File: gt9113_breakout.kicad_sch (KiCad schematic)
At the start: 10 parts, among them J6 504740-5100, J7 504740-5100, U9 GT9113

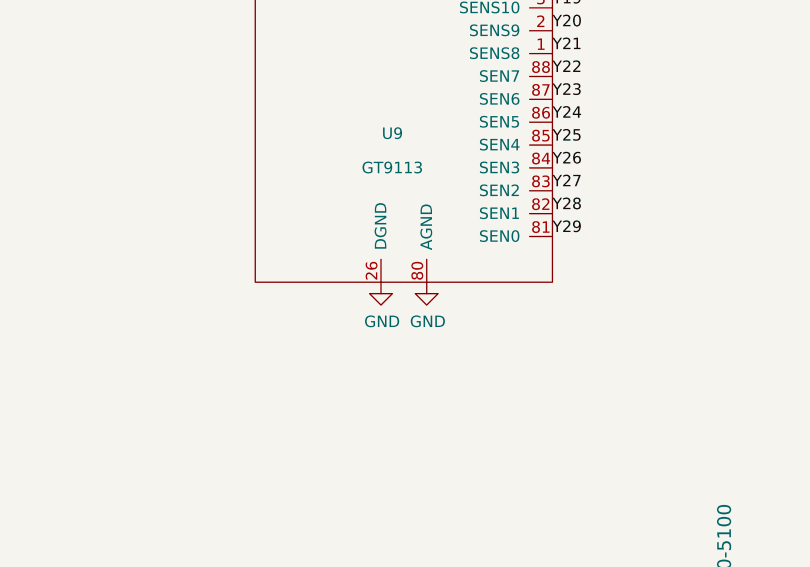
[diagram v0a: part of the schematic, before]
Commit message: Route CM4 board with differential connector on the right.
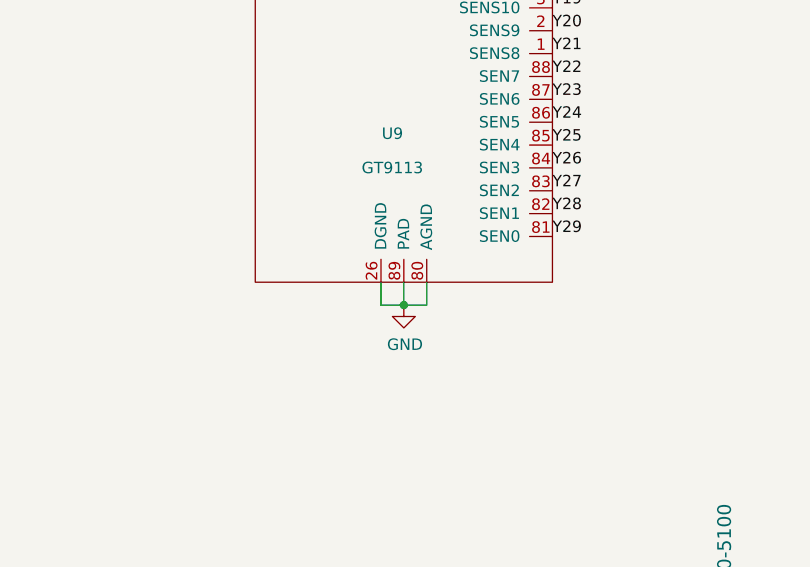
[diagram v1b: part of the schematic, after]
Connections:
- net GND: now also U9.89 (PAD)

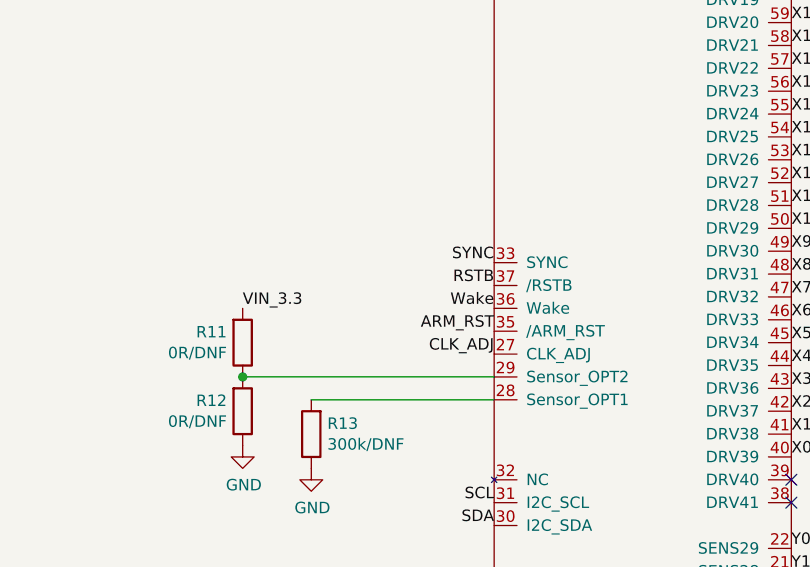
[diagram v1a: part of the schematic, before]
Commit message: Lots of tiny test points; add 3d models to a bunch of things. Re-length-match PCIe and DSI traces.
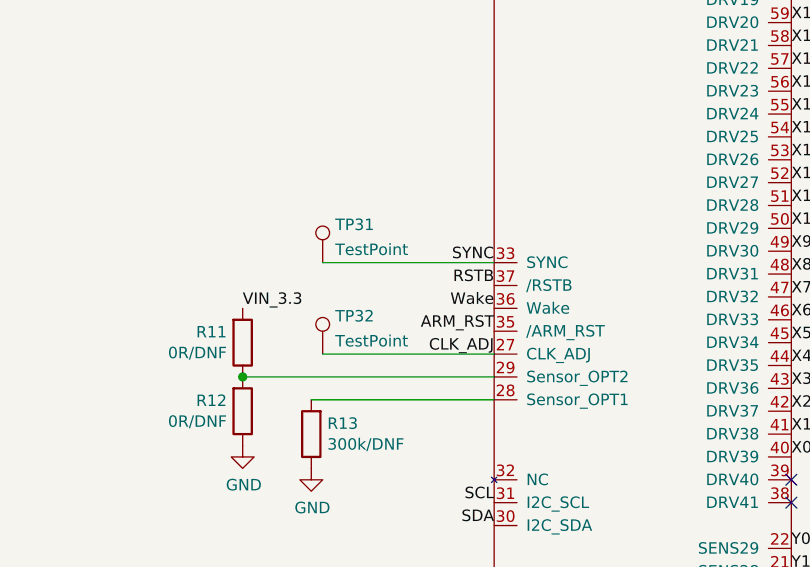
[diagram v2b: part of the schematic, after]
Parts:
- added TP31, TP32: TestPoint, footprints:testpoint_small, symbol Connector:TestPoint
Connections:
- net CLK_ADJ: now also TP32.1
- net SYNC: now also TP31.1
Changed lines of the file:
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@@
     (stroke (width 0) (type solid) (color 0 0 0 0))
+  )
+  (wire (pts (xy 214.63 137.16) (xy 233.68 137.16))
+    (stroke (width 0) (type default) (color 0 0 0 0))
   )
   (wire (pts (xy 247.65 44.45) (xy 247.65 24.13))
@@
   (wire (pts (xy 233.68 142.24) (xy 213.36 142.24))
     (stroke (width 0) (type solid) (color 0 0 0 0))
+  )
+  (wire (pts (xy 214.63 127) (xy 233.68 127))
+    (stroke (width 0) (type default) (color 0 0 0 0))
   )
   (wire (pts (xy 250.19 26.67) (xy 250.19 44.45))
@@
       (effects (font (size 1.27 1.27)) hide)
     )
+    (pin "1")
+  )
+  (symbol (lib_id "Connector:TestPoint") (at 214.63 127 0) (unit 1)
+    (in_bom yes) (on_board yes) (fields_autoplaced)
+    (property "Reference" "TP31" (id 0) (at 216.027 122.7895 0)
+      (effects (font (size 1.27 1.27)) (justify left))
+    )
+    (property "Value" "TestPoint" (id 1) (at 216.027 125.5646 0)
+      (effects (font (size 1.27 1.27)) (justify left))
+    )
+    (property "Footprint" "footprints:testpoint_small" (id 2) (at 219.71 127 0)
+      (effects (font (size 1.27 1.27)) hide)
+    )
+    (property "Datasheet" "~" (id 3) (at 219.71 127 0)
+      (effects (font (size 1.27 1.27)) hide)
+    )
+    (pin "1")
+  )
+  (symbol (lib_id "Connector:TestPoint") (at 214.63 137.16 0) (unit 1)
+    (in_bom yes) (on_board yes) (fields_autoplaced)
+    (property "Reference" "TP32" (id 0) (at 216.027 132.9495 0)
+      (effects (font (size 1.27 1.27)) (justify left))
+    )
+    (property "Value" "TestPoint" (id 1) (at 216.027 135.7246 0)
+      (effects (font (size 1.27 1.27)) (justify left))
+    )
+    (property "Footprint" "footprints:testpoint_small" (id 2) (at 219.71 137.16 0)
+      (effects (font (size 1.27 1.27)) hide)
+    )
+    (property "Datasheet" "~" (id 3) (at 219.71 137.16 0)
+      (effects (font (size 1.27 1.27)) hide)
+    )

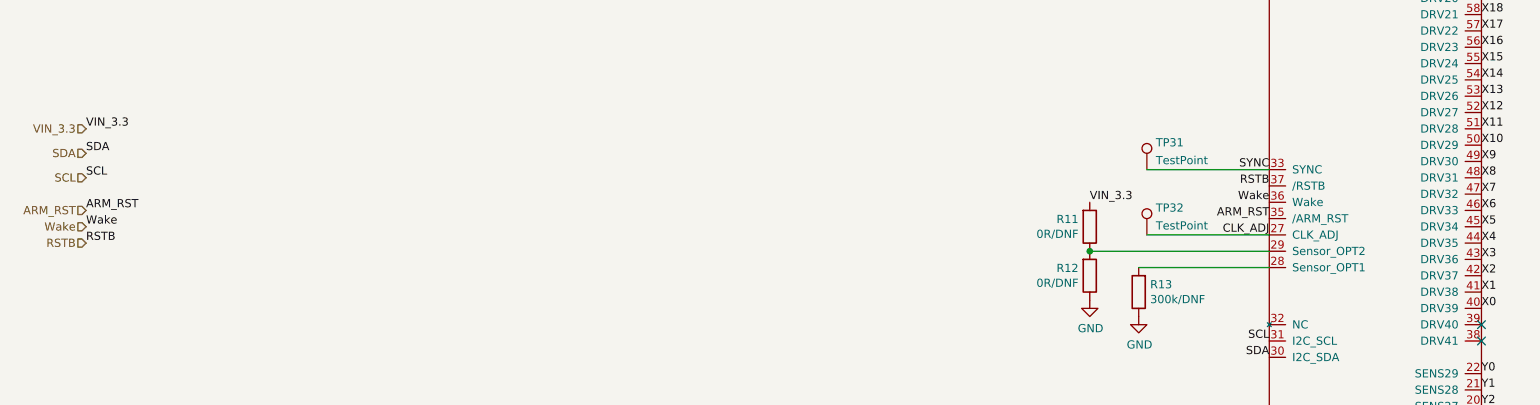
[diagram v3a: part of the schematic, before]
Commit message: Wire GT9110 INT pin to a GPIO, wire ARM_RST and Wake pins to test points instead of GPIOs. Add lots of test points, and footprints for status/power LEDs.
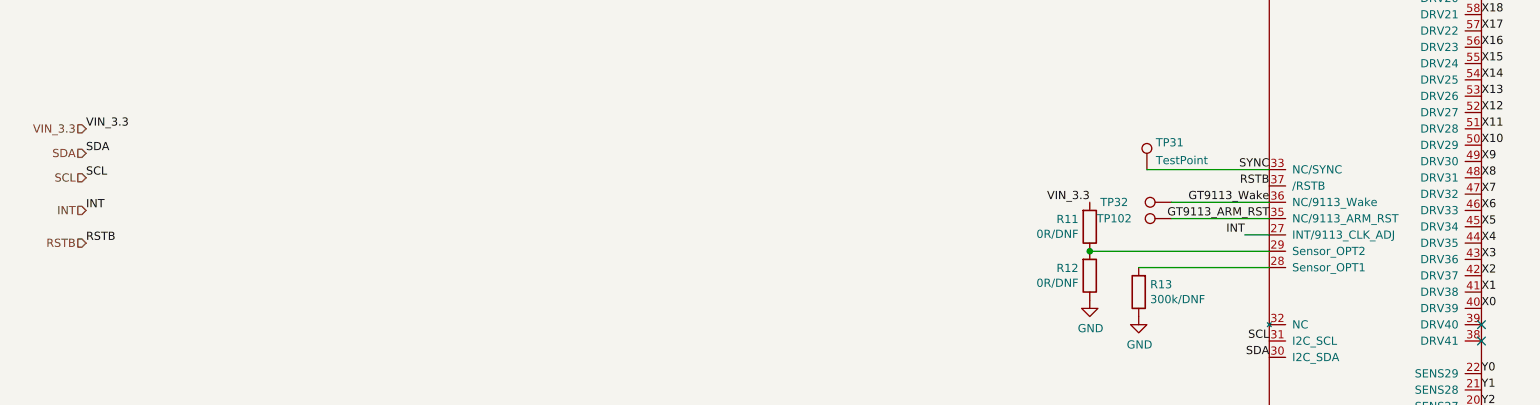
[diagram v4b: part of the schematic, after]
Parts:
- added TP102: TestPoint, footprints:testpoint_small, symbol Connector:TestPoint
- U9: symbol gt9113:GT9113 -> gt9113:GT9110
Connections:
- net Wake is gone; now on net GT9113_Wake: U9.36 (NC/9113_Wake)
- net ARM_RST renamed GT9113_ARM_RST
- net GT9113_ARM_RST: now also TP102.1
- net CLK_ADJ renamed GT9113_Wake
- net GT9113_Wake: no longer U9.27 (CLK_ADJ)
- new net INT: U9.27 (INT/9113_CLK_ADJ)
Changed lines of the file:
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@@
+    (stroke (width 0) (type default) (color 0 0 0 0))
+  )
+  (wire (pts (xy 218.44 134.62) (xy 233.68 134.62))
+    (stroke (width 0) (type default) (color 0 0 0 0))
+  )
+  (wire (pts (xy 229.87 137.16) (xy 233.68 137.16))
     (stroke (width 0) (type default) (color 0 0 0 0))
   )
@@
     (stroke (width 0) (type solid) (color 0 0 0 0))
   )
-  (wire (pts (xy 214.63 137.16) (xy 233.68 137.16))
-    (stroke (width 0) (type default) (color 0 0 0 0))
-  )
   (wire (pts (xy 247.65 44.45) (xy 247.65 24.13))
     (stroke (width 0) (type solid) (color 0 0 0 0))
@@
     (stroke (width 0) (type solid) (color 0 0 0 0))
   )
+  (wire (pts (xy 218.44 132.08) (xy 233.68 132.08))
+    (stroke (width 0) (type default) (color 0 0 0 0))
+  )
   (wire (pts (xy 214.63 127) (xy 233.68 127))
     (stroke (width 0) (type default) (color 0 0 0 0))
@@
     (effects (font (size 1.27 1.27)) (justify right bottom))
   )
+  (label "INT" (at 229.87 137.16 180)
+    (effects (font (size 1.27 1.27)) (justify right bottom))
+  )
   (label "Y26" (at 266.7 224.79 0)
     (effects (font (size 1.27 1.27)) (justify left bottom))
@@
     (effects (font (size 1.27 1.27)) (justify left bottom))
   )
-  (label "ARM_RST" (at 49.53 133.35 0)
-    (effects (font (size 1.27 1.27)) (justify left bottom))
-  )
   (label "Y11" (at 355.6 289.56 270)
     (effects (font (size 1.27 1.27)) (justify right bottom))
@@
     (effects (font (size 1.27 1.27)) (justify left bottom))
   )
+  (label "GT9113_ARM_RST" (at 233.68 134.62 180)
+    (effects (font (size 1.27 1.27)) (justify right bottom))
+  )
   (label "Y8" (at 111.76 289.56 270)
     (effects (font (size 1.27 1.27)) (justify right bottom))
@@
     (effects (font (size 1.27 1.27)) (justify left bottom))
   )
-  (label "ARM_RST" (at 233.68 134.62 180)
-    (effects (font (size 1.27 1.27)) (justify right bottom))
-  )
   (label "X27" (at 266.7 80.01 0)
     (effects (font (size 1.27 1.27)) (justify left bottom))
@@
     (effects (font (size 1.27 1.27)) (justify right bottom))
   )
-  (label "Wake" (at 49.53 135.89 0)
-    (effects (font (size 1.27 1.27)) (justify left bottom))
-  )
   (label "Y21" (at 266.7 212.09 0)
     (effects (font (size 1.27 1.27)) (justify left bottom))
@@
     (effects (font (size 1.27 1.27)) (justify left bottom))
   )
-  (label "Wake" (at 233.68 132.08 180)
-    (effects (font (size 1.27 1.27)) (justify right bottom))
-  )
   (label "X17" (at 266.7 105.41 0)
     (effects (font (size 1.27 1.27)) (justify left bottom))
@@
     (effects (font (size 1.27 1.27)) (justify left bottom))
   )
+  (label "GT9113_Wake" (at 233.68 132.08 180)
+    (effects (font (size 1.27 1.27)) (justify right bottom))
+  )
   (label "Y15" (at 345.44 289.56 270)
     (effects (font (size 1.27 1.27)) (justify right bottom))
@@
     (effects (font (size 1.27 1.27)) (justify right bottom))
   )
+  (label "INT" (at 49.53 133.35 0)
+    (effects (font (size 1.27 1.27)) (justify left bottom))
+  )
   (label "Y11" (at 266.7 186.69 0)
     (effects (font (size 1.27 1.27)) (justify left bottom))
@@
     (effects (font (size 1.27 1.27)) (justify right bottom))
   )
-  (label "CLK_ADJ" (at 233.68 137.16 180)
-    (effects (font (size 1.27 1.27)) (justify right bottom))
-  )
   (label "Y9" (at 266.7 181.61 0)
     (effects (font (size 1.27 1.27)) (justify left bottom))
@@
     (effects (font (size 1.27 1.27)) (justify right bottom))
   )
-  (label "VIN_3.3" (at 205.74 132.08 0)
-    (effects (font (size 1.27 1.27)) (justify left bottom))
+  (label "VIN_3.3" (at 205.74 132.08 180)
+    (effects (font (size 1.27 1.27)) (justify right bottom))
   )
   (label "Y5" (at 104.14 289.56 270)
@@
     (effects (font (size 1.27 1.27)) (justify left bottom))
   )
-  (hierarchical_label "ARM_RST" (shape input) (at 49.53 133.35 180)
+  (hierarchical_label "INT" (shape input) (at 49.53 133.35 180)
     (effects (font (size 1.27 1.27)) (justify right))
   )
@@
   )
   (hierarchical_label "VIN_3.3" (shape input) (at 49.53 120.65 180)
-    (effects (font (size 1.27 1.27)) (justify right))
-  )
-  (hierarchical_label "Wake" (shape input) (at 49.53 135.89 180)
     (effects (font (size 1.27 1.27)) (justify right))
   )
@@
     (pin "1")
   )
-  (symbol (lib_id "gt9113:GT9113") (at 250.19 140.97 0) (unit 1)
+  (symbol (lib_id "gt9113:GT9110") (at 250.19 140.97 0) (unit 1)
     (in_bom yes) (on_board yes)
     (property "Reference" "U9" (id 0) (at 248.92 220.98 0))
@@
       (effects (font (size 1.27 1.27)) hide)
     )
-    (property "Datasheet" "" (id 3) (at 248.92 127 0)
+    (property "Datasheet" "${KIPRJMOD}/datasheets/GT9110 Datasheet.pdf" (id 3) (at 240.03 96.52 90)
       (effects (font (size 1.27 1.27)) hide)
     )
@@
     (pin "1")
   )
+  (symbol (lib_id "Connector:TestPoint") (at 218.44 132.08 90) (unit 1)
+    (in_bom yes) (on_board yes)
+    (property "Reference" "TP32" (id 0) (at 209.55 132.08 90))
+    (property "Value" "TestPoint" (id 1) (at 215.138 130.2821 90)
+      (effects (font (size 1.27 1.27)) hide)
+    )
+    (property "Footprint" "footprints:testpoint_small" (id 2) (at 218.44 127 0)
+      (effects (font (size 1.27 1.27)) hide)
+    )
+    (property "Datasheet" "~" (id 3) (at 218.44 127 0)
+      (effects (font (size 1.27 1.27)) hide)
+    )
+    (pin "1")
+  )
   (symbol (lib_id "Connector:TestPoint") (at 214.63 127 0) (unit 1)
     (in_bom yes) (on_board yes) (fields_autoplaced)
@@
     (pin "1")
   )
-  (symbol (lib_id "Connector:TestPoint") (at 214.63 137.16 0) (unit 1)
-    (in_bom yes) (on_board yes) (fields_autoplaced)
-    (property "Reference" "TP32" (id 0) (at 216.027 132.9495 0)
-      (effects (font (size 1.27 1.27)) (justify left))
-    )
-    (property "Value" "TestPoint" (id 1) (at 216.027 135.7246 0)
-      (effects (font (size 1.27 1.27)) (justify left))
-    )
-    (property "Footprint" "footprints:testpoint_small" (id 2) (at 219.71 137.16 0)
-      (effects (font (size 1.27 1.27)) hide)
-    )
-    (property "Datasheet" "~" (id 3) (at 219.71 137.16 0)
-      (effects (font (size 1.27 1.27)) hide)
-    )
+  (symbol (lib_id "Connector:TestPoint") (at 218.44 134.62 90) (unit 1)
+    (in_bom yes) (on_board yes)
+    (property "Reference" "TP102" (id 0) (at 209.55 134.62 90))
+    (property "Value" "TestPoint" (id 1) (at 215.138 132.8221 90)
+      (effects (font (size 1.27 1.27)) hide)
+    )
+    (property "Footprint" "footprints:testpoint_small" (id 2) (at 218.44 129.54 0)
+      (effects (font (size 1.27 1.27)) hide)
+    )
+    (property "Datasheet" "~" (id 3) (at 218.44 129.54 0)
+      (effects (font (size 1.27 1.27)) hide)
+    )

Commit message: Board rev2 ready to order, hopefully
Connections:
- net AVDD18: now reaches C26.1, U9.24 (AVDD18)
- net DVDD12: now reaches C25.1, U9.25 (DVDD12)
- net Sensor_OPT2: now reaches R13.2, U9.28 (Sensor_OPT1)
- net Sensor_OPT1: now reaches R11.1, R12.2, U9.29 (Sensor_OPT2)
